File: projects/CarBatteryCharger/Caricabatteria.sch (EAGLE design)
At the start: 18 parts, among them T1 TAG 665-100, X1 MKDSN1,5/2-5,08, X2 MKDSN1,5/2-5,08, X3 MKDSN1,5/2-5,08

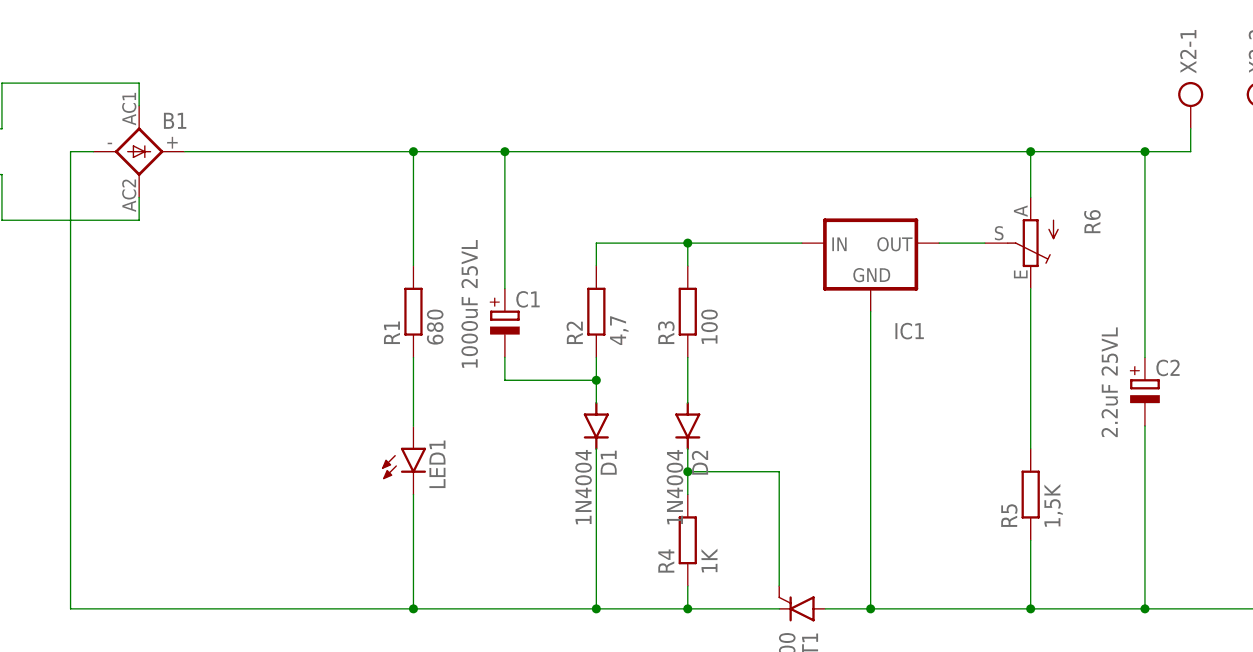
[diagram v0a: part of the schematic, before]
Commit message: Correct value of some component
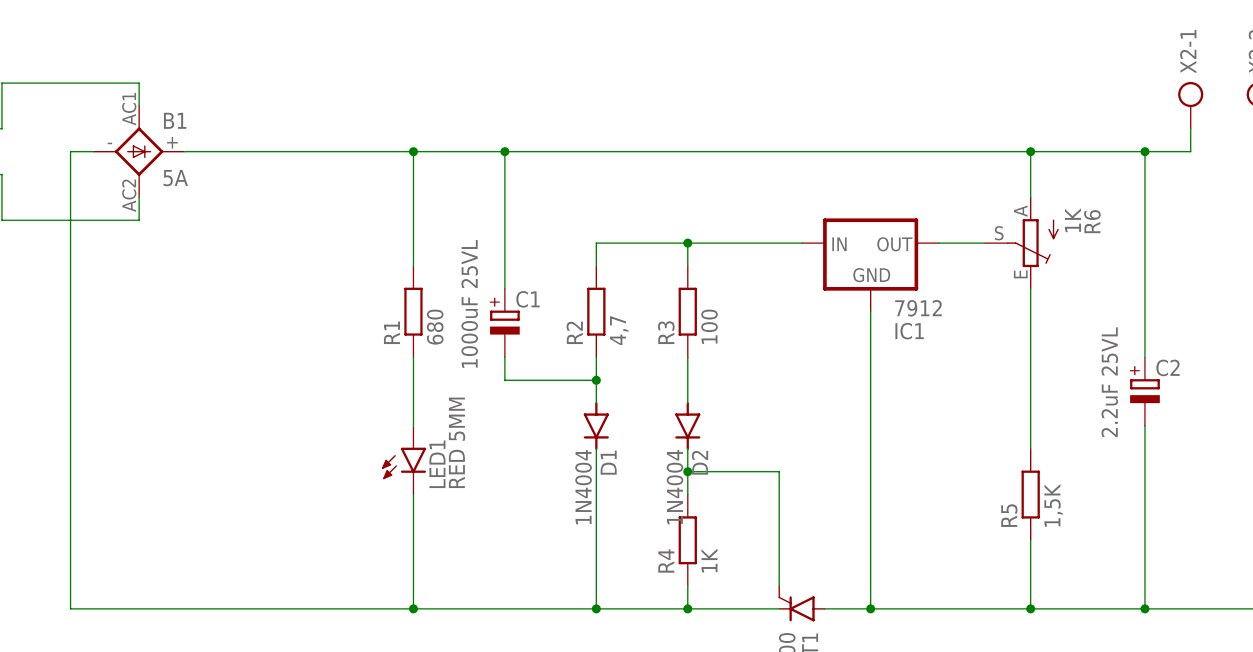
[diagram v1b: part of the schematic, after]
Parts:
- B1: value (none) -> 5A
- IC1: value (none) -> 7912
- LED1: value (none) -> RED 5MM
- R6: value (none) -> 1K
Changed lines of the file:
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@@
 </classes>
 <parts>
-<part name="B1" library="rectifier-IZ0VLL" deviceset="SKB" device="" package3d_urn="urn:adsk.eagle:package:23874/1"/>
+<part name="B1" library="rectifier-IZ0VLL" deviceset="SKB" device="" package3d_urn="urn:adsk.eagle:package:23874/1" value="5A"/>
 <part name="R1" library="rcl-IZ0VLL" deviceset="R-EU_" device="0207/10" package3d_urn="urn:adsk.eagle:package:23491/2" value="680"/>
 <part name="R2" library="rcl-IZ0VLL" deviceset="R-EU_" device="0207/10" package3d_urn="urn:adsk.eagle:package:23491/2" value="4,7"/>
@@
 <part name="R4" library="rcl-IZ0VLL" deviceset="R-EU_" device="0207/10" package3d_urn="urn:adsk.eagle:package:23491/2" value="1K"/>
 <part name="R5" library="rcl-IZ0VLL" deviceset="R-EU_" device="0207/10" package3d_urn="urn:adsk.eagle:package:23491/2" value="1,5K"/>
-<part name="LED1" library="led-IZ0VLL" deviceset="LED" device="5MM" package3d_urn="urn:adsk.eagle:package:15799/2"/>
+<part name="LED1" library="led-IZ0VLL" deviceset="LED" device="5MM" package3d_urn="urn:adsk.eagle:package:15799/2" value="RED 5MM"/>
 <part name="D1" library="diode-IZ0VLL" deviceset="1N4004" device="" package3d_urn="urn:adsk.eagle:package:43336/1"/>
 <part name="D2" library="diode-IZ0VLL" deviceset="1N4004" device="" package3d_urn="urn:adsk.eagle:package:43336/1"/>
-<part name="IC1" library="v-reg" library_urn="urn:adsk.eagle:library:409" deviceset="79XXS" device="" package3d_urn="urn:adsk.eagle:package:30343/1"/>
+<part name="IC1" library="v-reg" library_urn="urn:adsk.eagle:library:409" deviceset="79XXS" device="" package3d_urn="urn:adsk.eagle:package:30343/1" value="7912"/>
 <part name="T1" library="triac" library_urn="urn:adsk.eagle:library:403" deviceset="TIC126" device="" package3d_urn="urn:adsk.eagle:package:30140/2" value="TAG 665-100"/>
-<part name="R6" library="pot" library_urn="urn:adsk.eagle:library:331" deviceset="TRIM_EU-" device="PT10S" package3d_urn="urn:adsk.eagle:package:22711/1"/>
+<part name="R6" library="pot" library_urn="urn:adsk.eagle:library:331" deviceset="TRIM_EU-" device="PT10S" package3d_urn="urn:adsk.eagle:package:22711/1" value="1K"/>
 <part name="C1" library="rcl-IZ0VLL" deviceset="CPOL-EU" device="E5-10.5" package3d_urn="urn:adsk.eagle:package:23372/2" value="1000uF 25VL"/>
 <part name="C2" library="rcl-IZ0VLL" deviceset="CPOL-EU" device="E5-10.5" package3d_urn="urn:adsk.eagle:package:23372/2" value="2.2uF 25VL"/>
